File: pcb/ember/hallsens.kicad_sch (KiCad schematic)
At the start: 68 parts, among them IC1 ADG708BRUZ-REEL7, IC2 ADG708BRUZ-REEL7, IC3 ADG708BRUZ-REEL7, IC4 ADG708BRUZ-REEL7, U10 Hall_Sensor, U11 Hall_Sensor, U12 Hall_Sensor, U13 Hall_Sensor, U14 Hall_Sensor, U15 Hall_Sensor, U16 Hall_Sensor, U17 Hall_Sensor, U18 Hall_Sensor, U19 Hall_Sensor, U2 Hall_Sensor, U20 Hall_Sensor, U21 Hall_Sensor, U22 Hall_Sensor, U23 Hall_Sensor, U24 Hall_Sensor, U25 Hall_Sensor, U26 Hall_Sensor, U27 Hall_Sensor, U28 Hall_Sensor, U29 Hall_Sensor, U3 Hall_Sensor, U30 Hall_Sensor, U31 Hall_Sensor, U32 Hall_Sensor, U33 Hall_Sensor, U4 Hall_Sensor, U5 Hall_Sensor, U6 Hall_Sensor, U7 Hall_Sensor, U8 Hall_Sensor, U9 Hall_Sensor

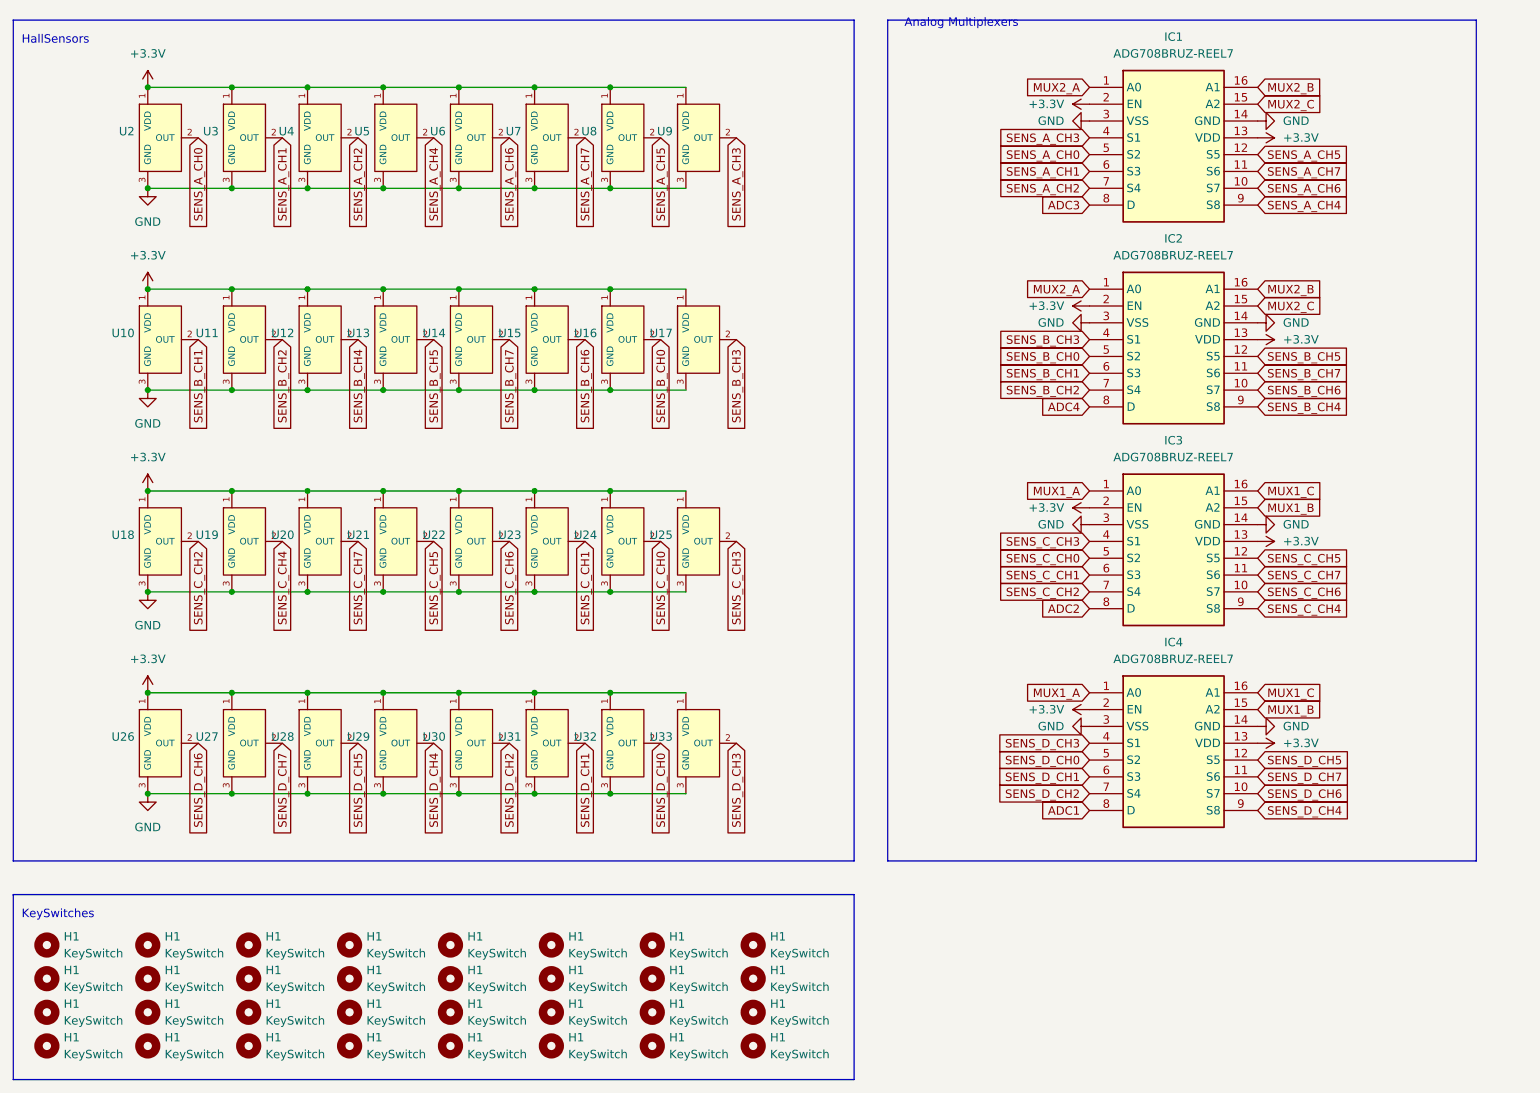
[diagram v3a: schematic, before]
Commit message: :sparkles: add bypass cap
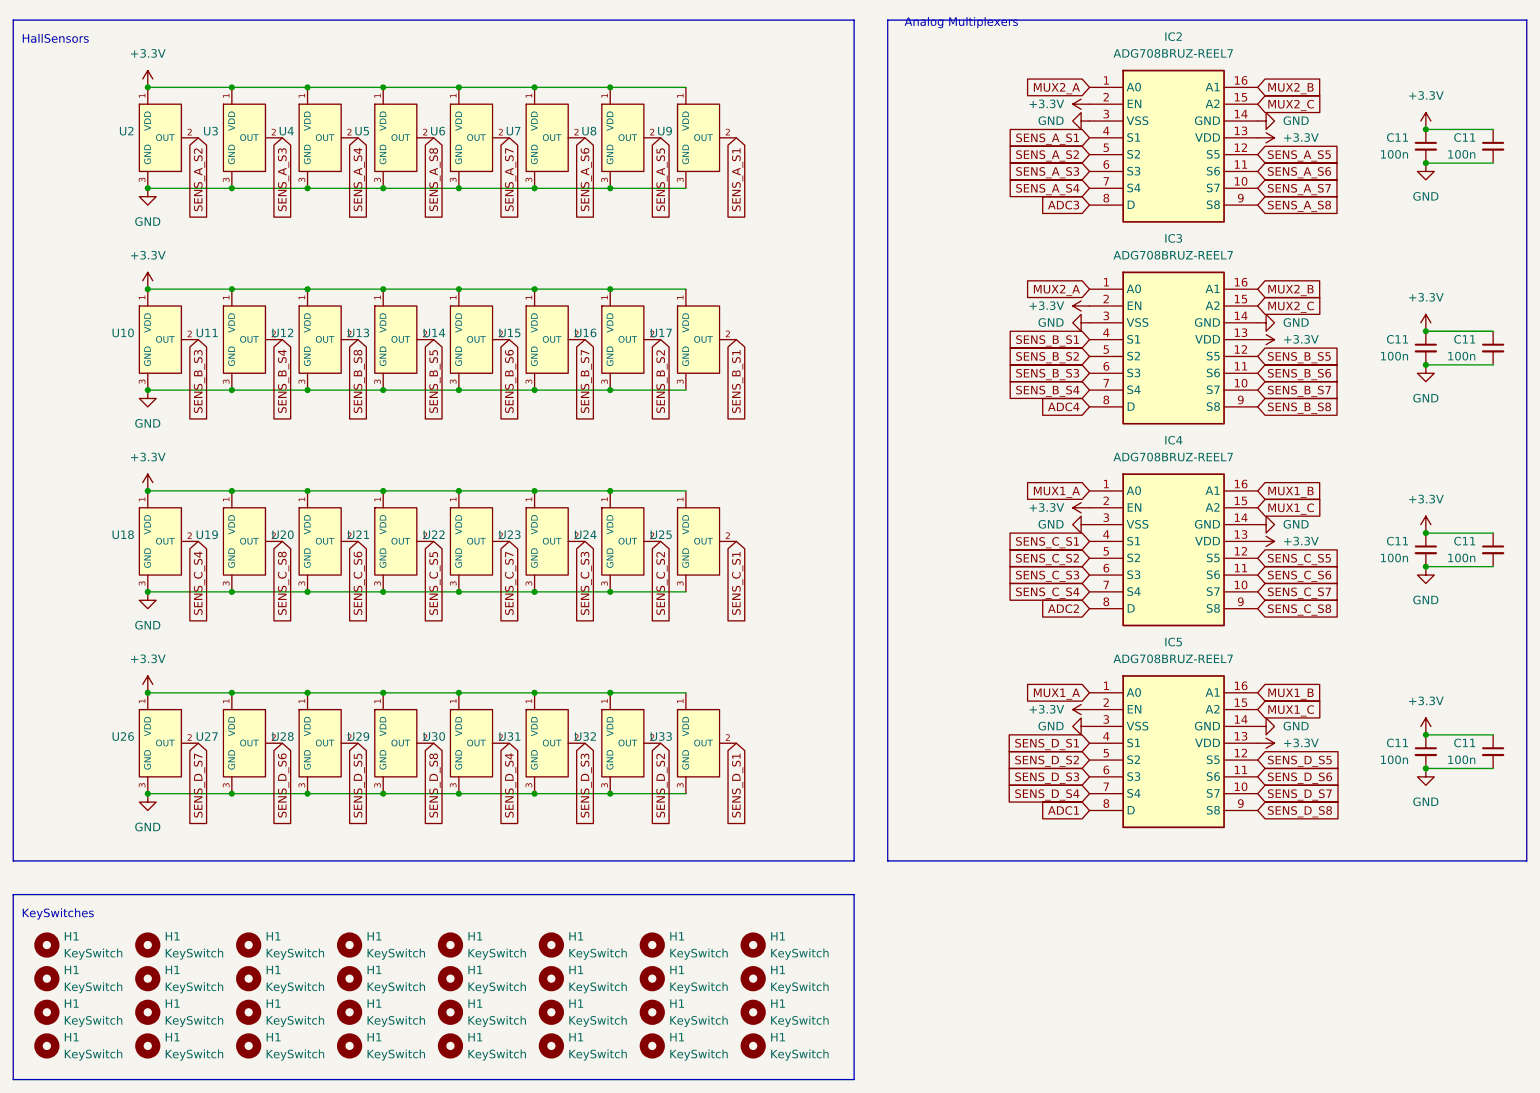
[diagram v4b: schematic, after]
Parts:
- added C11 (x8): 100n, Capacitor_SMD:C_0603_1608Metric, symbol Device:C_Small
- renumbered IC1 to IC2, IC2 to IC3, IC3 to IC4, IC4 to IC5
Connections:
- net +3.3V: now also C11.1, C11.1, C11.1, C11.1, C11.1, C11.1, C11.1, C11.1
- net GND: now also C11.2, C11.2, C11.2, C11.2, C11.2, C11.2, C11.2, C11.2
- net MUX1_B: now also IC4.16 (A1), IC5.16 (A1); no longer IC4.15 (A2), IC5.15 (A2)
- net MUX1_C: now also IC4.15 (A2), IC5.15 (A2); no longer IC4.16 (A1), IC5.16 (A1)
- net SENS_A_CH0 renamed SENS_A_S2
- net SENS_A_CH1 renamed SENS_A_S3
- net SENS_A_CH2 renamed SENS_A_S4
- net SENS_A_CH3 renamed SENS_A_S1
- net SENS_A_CH4 renamed SENS_A_S8
- net SENS_A_CH5 renamed SENS_A_S5
- net SENS_A_CH6 renamed SENS_A_S7
- net SENS_A_CH7 renamed SENS_A_S6
- net SENS_B_CH0 renamed SENS_B_S2
- net SENS_B_CH1 renamed SENS_B_S3
- net SENS_B_CH2 renamed SENS_B_S4
- net SENS_B_CH3 renamed SENS_B_S1
- net SENS_B_CH4 renamed SENS_B_S8
- net SENS_B_CH5 renamed SENS_B_S5
- net SENS_B_CH6 renamed SENS_B_S7
- net SENS_B_CH7 renamed SENS_B_S6
- net SENS_C_CH0 renamed SENS_C_S2
- net SENS_C_CH1 renamed SENS_C_S3
- net SENS_C_CH2 renamed SENS_C_S4
- net SENS_C_CH3 renamed SENS_C_S1
- net SENS_C_CH4 renamed SENS_C_S8
- net SENS_C_CH5 renamed SENS_C_S5
- net SENS_C_CH6 renamed SENS_C_S7
- net SENS_C_CH7 renamed SENS_C_S6
- net SENS_D_CH0 renamed SENS_D_S2
- net SENS_D_CH1 renamed SENS_D_S3
- net SENS_D_CH2 renamed SENS_D_S4
- net SENS_D_CH3 renamed SENS_D_S1
- net SENS_D_CH4 renamed SENS_D_S8
- net SENS_D_CH5 renamed SENS_D_S5
- net SENS_D_CH6 renamed SENS_D_S7
- net SENS_D_CH7 renamed SENS_D_S6

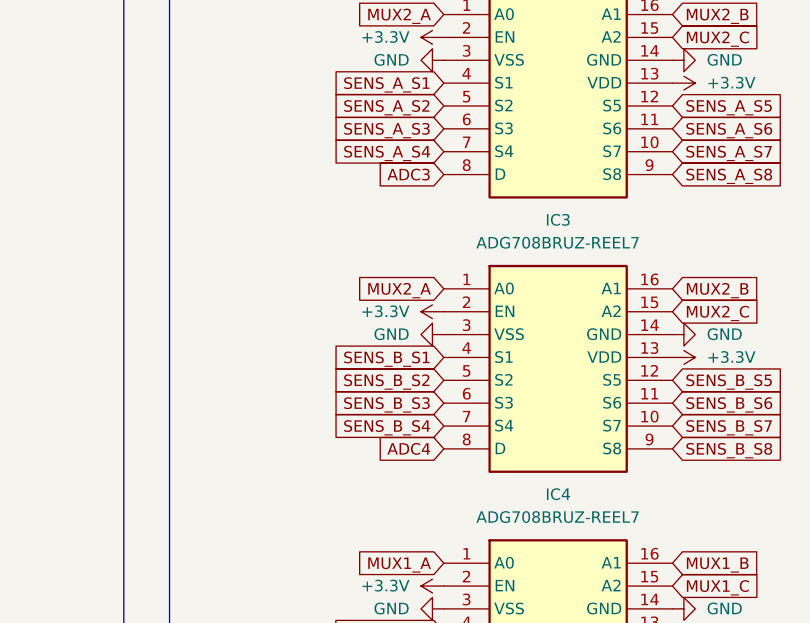
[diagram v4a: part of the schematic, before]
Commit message: :sparkles: opampを使ってのADCに切り替えられるようにピンアサインを変更
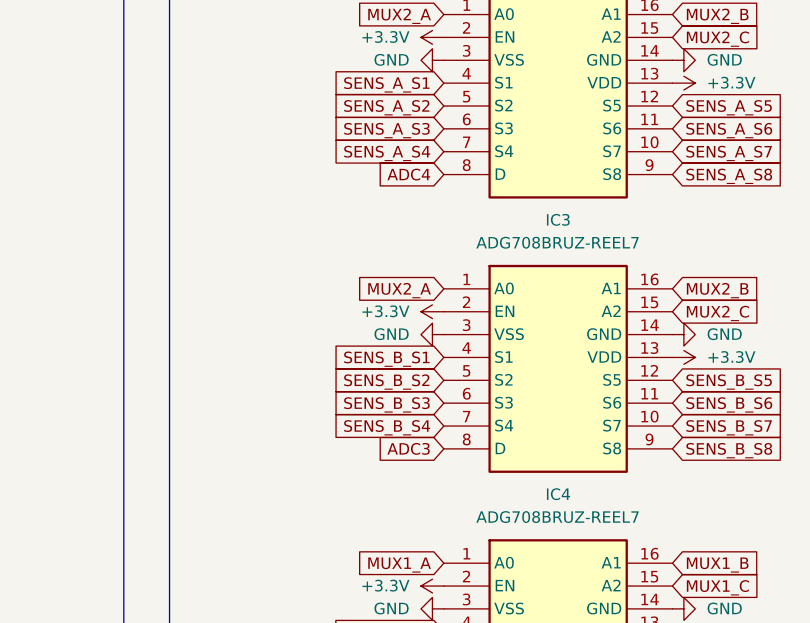
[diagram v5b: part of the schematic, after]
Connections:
- net ADC3: now also IC3.8 (D); no longer IC2.8 (D)
- net ADC4: now also IC2.8 (D); no longer IC3.8 (D)
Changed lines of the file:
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@@
     )
   )
-  (global_label "ADC4" (shape input) (at 200.66 83.82 180) (fields_autoplaced)
+  (global_label "ADC4" (shape input) (at 200.66 53.34 180) (fields_autoplaced)
     (effects (font (size 1.27 1.27)) (justify right))
-    (property "Intersheetrefs" "${INTERSHEET_REFS}" (at 192.8367 83.82 0)
+    (property "Intersheetrefs" "${INTERSHEET_REFS}" (at 192.8367 53.34 0)
       (effects (font (size 1.27 1.27)) (justify right) hide)
     )
@@
     )
   )
-  (global_label "ADC3" (shape input) (at 200.66 53.34 180) (fields_autoplaced)
+  (global_label "ADC3" (shape input) (at 200.66 83.82 180) (fields_autoplaced)
     (effects (font (size 1.27 1.27)) (justify right))
-    (property "Intersheetrefs" "${INTERSHEET_REFS}" (at 192.8367 53.34 0)
+    (property "Intersheetrefs" "${INTERSHEET_REFS}" (at 192.8367 83.82 0)
       (effects (font (size 1.27 1.27)) (justify right) hide)
     )
